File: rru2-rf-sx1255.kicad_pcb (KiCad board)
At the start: 4 copper layers, 0 parts

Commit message: Add a preliminary M.2 2230 key E board outline
The outline is a copy of the KiCad footprint Connector_PCBEdge:M.2_2230-xx-E. The card size is not decided yet.
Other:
- board outline added: 22 x 30 mm
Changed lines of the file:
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@@
 		)
+	)
+	(gr_line
+		(start 89 104)
+		(end 89 130)
+		(stroke
+			(width 0.2)
+			(type solid)
+		)
+		(layer "Edge.Cuts")
+	)
+	(gr_line
+		(start 89 130)
+		(end 89.575 130)
+		(stroke
+			(width 0.2)
+			(type solid)
+		)
+		(layer "Edge.Cuts")
+	)
+	(gr_arc
+		(start 89.575 130)
+		(mid 89.9286 130.146)
+		(end 90.075 130.5)
+		(stroke
+			(width 0.2)
+			(type solid)
+		)
+		(layer "Edge.Cuts")
+	)
+	(gr_line
+		(start 90.075 130.5)
+		(end 90.075 134)
+		(stroke
+			(width 0.2)
+			(type solid)
+		)
+		(layer "Edge.Cuts")
+	)
+	(gr_line
+		(start 90.075 134)
+		(end 102.025 134)
+		(stroke
+			(width 0.2)
+			(type solid)
+		)
+		(layer "Edge.Cuts")
+	)
+	(gr_line
+		(start 98.25 104)
+		(end 89 104)
+		(stroke
+			(width 0.2)
+			(type solid)
+		)
+		(layer "Edge.Cuts")
+	)
+	(gr_arc
+		(start 101.75 104)
+		(mid 100 105.75)
+		(end 98.25 104)
+		(stroke
+			(width 0.2)
+			(type solid)
+		)
+		(layer "Edge.Cuts")
+	)
+	(gr_arc
+		(start 102.025 130.5)
+		(mid 102.625 129.9)
+		(end 103.225 130.5)
+		(stroke
+			(width 0.2)
+			(type solid)
+		)
+		(layer "Edge.Cuts")
+	)
+	(gr_line
+		(start 102.025 134)
+		(end 102.025 130.5)
+		(stroke
+			(width 0.2)
+			(type solid)
+		)
+		(layer "Edge.Cuts")
+	)
+	(gr_line
+		(start 103.225 130.5)
+		(end 103.225 134)
+		(stroke
+			(width 0.2)
+			(type solid)
+		)
+		(layer "Edge.Cuts")
+	)
+	(gr_line
+		(start 103.225 134)
+		(end 109.925 134)
+		(stroke
+			(width 0.2)
+			(type solid)
+		)
+		(layer "Edge.Cuts")
+	)
+	(gr_arc
+		(start 109.925 130.5)
+		(mid 110.071 130.146)
+		(end 110.425 130)
+		(stroke
+			(width 0.2)
+			(type solid)
+		)
+		(layer "Edge.Cuts")
+	)
+	(gr_line
+		(start 109.925 134)
+		(end 109.925 130.5)
+		(stroke
+			(width 0.2)
+			(type solid)
+		)
+		(layer "Edge.Cuts")
+	)
+	(gr_line
+		(start 110.425 130)
+		(end 111 130)
+		(stroke
+			(width 0.2)
+			(type solid)
+		)
+		(layer "Edge.Cuts")
+	)
+	(gr_line
+		(start 111 104)
+		(end 101.75 104)
+		(stroke
+			(width 0.2)
+			(type solid)
+		)
+		(layer "Edge.Cuts")
+	)
+	(gr_line
+		(start 111 130)
+		(end 111 104)
+		(stroke
+			(width 0.2)
+			(type solid)
+		)
+		(layer "Edge.Cuts")
 	)
 	(embedded_fonts no)

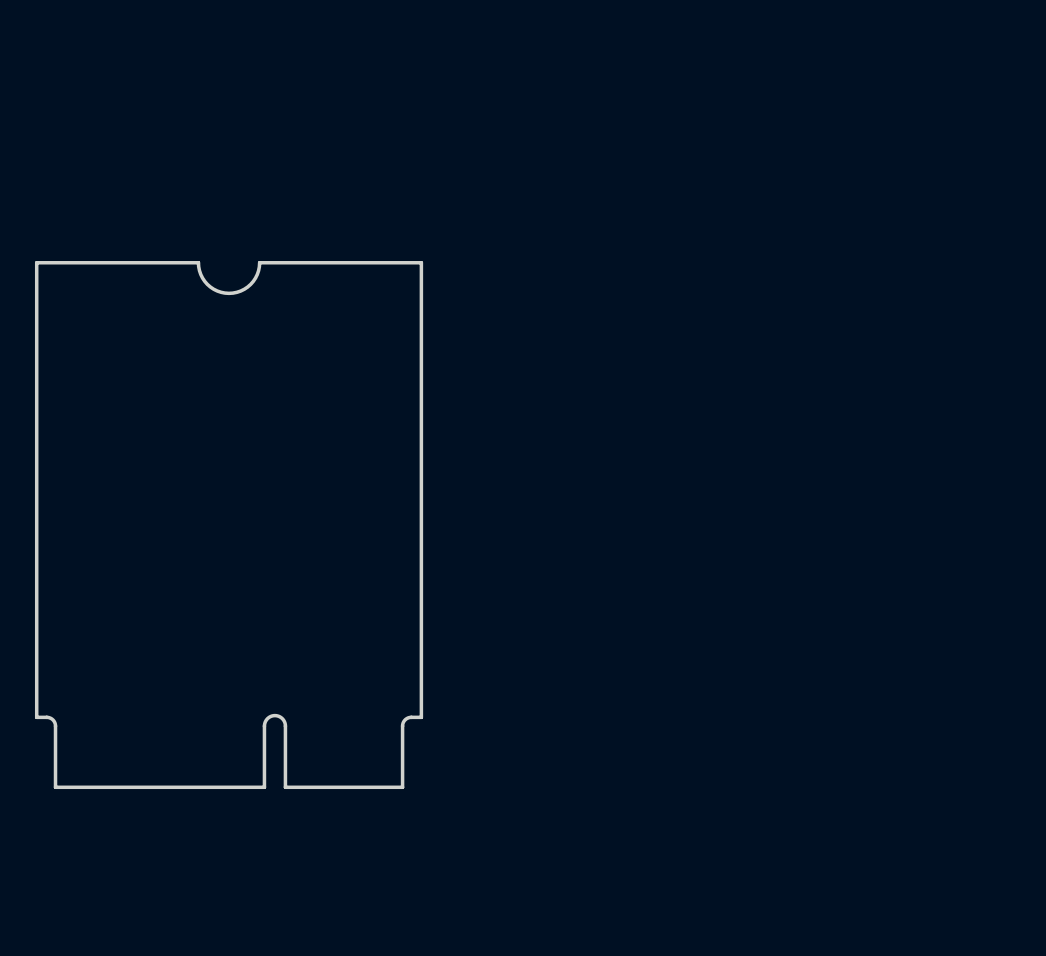
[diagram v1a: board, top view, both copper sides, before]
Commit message: Add the basic SX1255 schematic and the footprints
- The SX1255 block, the ferrite bead supply and the ID EEPROM use the
  circuit of the SX1255 HAT: decoupling, TCXO clock into XTB, series
  resistors on SPI and I2S, test points on DIO0, DIO1 and DIO3.
- RX: U.FL, DC block and L match to RFI. TX: RFO_P through 33 pF to U.FL.
- Preliminary M.2 key E pinout (text on the schematic).
- Authors in the title blocks.
- The footprints are on the board. They are not placed and not routed.
- The board is marked as work in progress (KiCad text variable WIP_MARK).
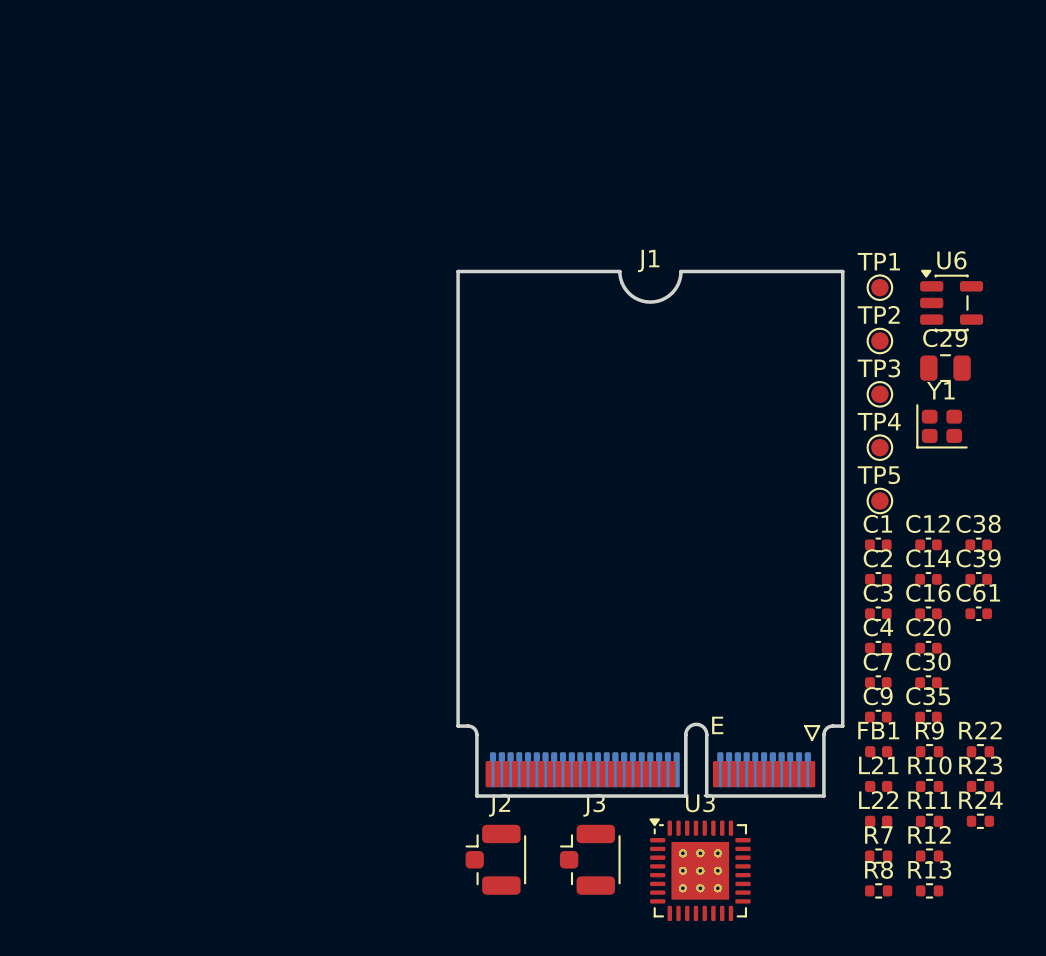
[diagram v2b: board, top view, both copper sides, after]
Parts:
- added C1: 1uF, Capacitor_SMD:C_0402_1005Metric, F.Cu at (137.1, 120.1)
- added C12: 100nF, Capacitor_SMD:C_0402_1005Metric, F.Cu at (140.0, 120.1)
- added C14: 100nF, Capacitor_SMD:C_0402_1005Metric, F.Cu at (140.0, 122.1)
- added C16: 33pF, Capacitor_SMD:C_0402_1005Metric, F.Cu at (140.0, 124.1)
- added C2: 100nF, Capacitor_SMD:C_0402_1005Metric, F.Cu at (137.1, 122.1)
- added C20: 27pF, Capacitor_SMD:C_0402_1005Metric, F.Cu at (140.0, 126.0)
- added C29: 10uF, Capacitor_SMD:C_0805_2012Metric, F.Cu at (141.0, 110.0)
- added C3: 1uF, Capacitor_SMD:C_0402_1005Metric, F.Cu at (137.1, 124.1)
- added C30: 100nF, Capacitor_SMD:C_0402_1005Metric, F.Cu at (140.0, 128.0)
- added C35: 100nF, Capacitor_SMD:C_0402_1005Metric, F.Cu at (140.0, 130.0)
- added C38: 1uF, Capacitor_SMD:C_0402_1005Metric, F.Cu at (142.9, 120.1)
- added C39: 100pF, Capacitor_SMD:C_0402_1005Metric, F.Cu at (142.9, 122.1)
- added C4: 1uF, Capacitor_SMD:C_0402_1005Metric, F.Cu at (137.1, 126.0)
- added C61: 100pF, Capacitor_SMD:C_0402_1005Metric, F.Cu at (142.9, 124.1)
- added C7: 100nF, Capacitor_SMD:C_0402_1005Metric, F.Cu at (137.1, 128.0)
- added C9: 100nF, Capacitor_SMD:C_0402_1005Metric, F.Cu at (137.1, 130.0)
- added FB1: 600R@100MHz, Inductor_SMD:L_0402_1005Metric, F.Cu at (137.2, 132.0)
- added J1: M.2 key E, Connector_PCBEdge:M.2_2230-xx-E, F.Cu at (124.1, 130.5)
- added J2: U.FL-R-SMT-1(60), Connector_Coaxial:U.FL_Hirose_U.FL-R-SMT-1_Vertical, F.Cu at (115.6, 138.1)
- added J3: U.FL-R-SMT-1(60), Connector_Coaxial:U.FL_Hirose_U.FL-R-SMT-1_Vertical, F.Cu at (121.0, 138.1)
- added L21: 39nH, Inductor_SMD:L_0402_1005Metric, F.Cu at (137.2, 134.0)
- added L22: 82nH, Inductor_SMD:L_0402_1005Metric, F.Cu at (137.2, 135.9)
- added R10: 120R, Resistor_SMD:R_0402_1005Metric, F.Cu at (140.1, 134.0)
- added R11: 120R, Resistor_SMD:R_0402_1005Metric, F.Cu at (140.1, 135.9)
- added R12: 120R, Resistor_SMD:R_0402_1005Metric, F.Cu at (140.1, 137.9)
- added R13: 120R, Resistor_SMD:R_0402_1005Metric, F.Cu at (140.1, 139.9)
- added R22: 10k, Resistor_SMD:R_0402_1005Metric, F.Cu at (143.0, 132.0)
- added R23: 10k, Resistor_SMD:R_0402_1005Metric, F.Cu at (143.0, 134.0)
- added R24: 10k, Resistor_SMD:R_0402_1005Metric, F.Cu at (143.0, 135.9)
- added R7: 120R, Resistor_SMD:R_0402_1005Metric, F.Cu at (137.2, 137.9)
- added R8: 120R, Resistor_SMD:R_0402_1005Metric, F.Cu at (137.2, 139.9)
- added R9: 120R, Resistor_SMD:R_0402_1005Metric, F.Cu at (140.1, 132.0)
- added TP1: TestPoint, TestPoint:TestPoint_Pad_D1.0mm, F.Cu at (137.2, 105.4)
- added TP2: TestPoint, TestPoint:TestPoint_Pad_D1.0mm, F.Cu at (137.2, 108.5)
- added TP3: TestPoint, TestPoint:TestPoint_Pad_D1.0mm, F.Cu at (137.2, 111.5)
- added TP4: TestPoint, TestPoint:TestPoint_Pad_D1.0mm, F.Cu at (137.2, 114.6)
- added TP5: TestPoint, TestPoint:TestPoint_Pad_D1.0mm, F.Cu at (137.2, 117.6)
- added U3: SX1255, Package_DFN_QFN:QFN-32-1EP_5x5mm_P0.5mm_EP3.3x3.3mm_ThermalVias, F.Cu at (127.0, 138.8)
- added U6: AT24C32D, Package_TO_SOT_SMD:SOT-23-5, F.Cu at (141.3, 106.3)
- added Y1: 32MHz, Crystal:Crystal_SMD_2016-4Pin_2.0x1.6mm, F.Cu at (140.8, 113.4)

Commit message: Place the RF parts and add the 32 MHz VCXO
This is work in progress. The board has no tracks yet.

- Change the card size to M.2 2242 key E for the shield.
- Place the SX1255 near the middle of the card.
- Place the crystal, the capacitors and the supply filter near the SX1255.
- Put the two U.FL connectors near the screw end on opposite sides.
- Put the test pads on the bottom side.
- Add zones for the HMC374, the PE4312 attenuators and the ADF4002.
- Connect DIO0, DIO1 and DIO3 of the SX1255 to the M.2 pins 21, 20 and 16.
- Replace the TCXO with the Renesas XLH53V032 VCXO for the ADF4002 PLL.
- Add a 1k and 470R divider between the VCXO output and XTB.
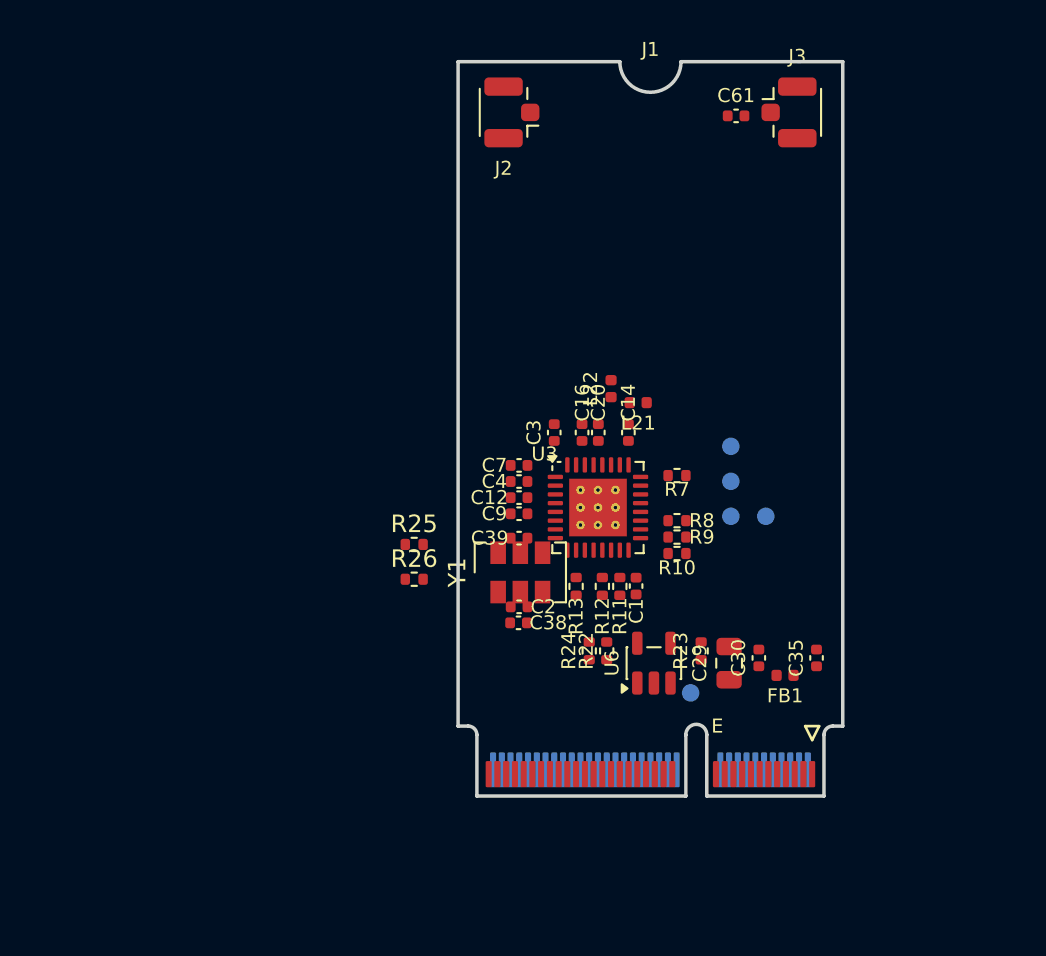
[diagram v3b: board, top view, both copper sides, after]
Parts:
- added R25: 1k, Resistor_SMD:R_0402_1005Metric, F.Cu at (110.6, 120.1)
- added R26: 470R, Resistor_SMD:R_0402_1005Metric, F.Cu at (110.6, 122.1)
- J1: footprint Connector_PCBEdge:M.2_2230-xx-E -> M17_Connectors:M.2_2242-xx-E
- TP1, TP2, TP3, TP4, TP5: moved to B.Cu
- Y1: footprint Crystal:Crystal_SMD_2016-4Pin_2.0x1.6mm -> Oscillator:Oscillator_SMD_IDT_JS6-6_5.0x3.2mm_P1.27mm
- moved J3 44.3 mm to (132.5, 95.4)
- moved J2 42.7 mm to (115.7, 95.4), turned to 180 degrees
- moved C61 31.7 mm to (129.0, 95.6)
- moved L22 29.1 mm to (121.8, 111.2), turned to 90 degrees
- moved U6 26.7 mm to (124.3, 126.9), turned to 90 degrees
- moved C38 26.7 mm to (116.6, 124.6)
- moved R13 26.7 mm to (119.8, 122.5), turned to -90 degrees
- moved C39 26.4 mm to (116.6, 119.8), turned to 180 degrees
- moved L21 25.9 mm to (123.4, 112.0), turned to 180 degrees
- moved Y1 25.5 mm to (116.7, 121.7), turned to 90 degrees
- moved R7 24.6 mm to (125.6, 116.2)
- moved R24 24.4 mm to (120.6, 126.2), turned to 90 degrees
- moved R12 24.3 mm to (121.3, 122.5), turned to -90 degrees
- moved R8 24.1 mm to (125.6, 118.8)
- moved C7 24.0 mm to (116.6, 115.6), turned to 180 degrees
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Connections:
- C39 pad 2: Net-(Y1-OUT) -> Net-(C39-Pad2)
- J1 pad 16: unconnected-(J1-~{LED_2}-Pad16) -> /SX_DIO3
- J1 pad 20: unconnected-(J1-~{UART_WAKE}-Pad20) -> /SX_DIO1
- J1 pad 21: unconnected-(J1-~{SDIO_WAKE}-Pad21) -> /SX_DIO0
- TP1 pad 1: Net-(U3-DIO3) -> /SX_DIO3
- TP2 pad 1: Net-(U3-DIO1) -> /SX_DIO1
- TP3 pad 1: Net-(U3-DIO0) -> /SX_DIO0
- U3 pad 21: Net-(U3-DIO0) -> /SX_DIO0
- U3 pad 22: Net-(U3-DIO1) -> /SX_DIO1
- U3 pad 24: Net-(U3-DIO3) -> /SX_DIO3
- Y1 pad 1: GND -> /VCXO_VC
- Y1 pad 2: GND -> +3V3_RF
- Y1 pad 3: Net-(Y1-OUT) -> GND
- Y1 pad 4: +3V3_RF -> Net-(Y1-OUT)
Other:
- board size 22 x 30 mm -> 22 x 42 mm
- board text added: "3x PE4312"
- board text added: "ADF4002"
- board text added: "HMC374"
